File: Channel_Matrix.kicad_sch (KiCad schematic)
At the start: 0 parts

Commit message: progress on switch sheet
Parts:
- added R1601, R1602, R1603, R1604, R1901, R1902, R1903, R1904, R2001, R2101, R2102: 0R, symbol Device:R_Small
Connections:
- net Channel_1: now also R1603.2
- net Channel_2: now also R1604.2
- net Channel_3v3_1: now also R1601.2
- net Channel_3v3_2: now also R1602.2
- net Channel_5V_1: now also R1902.2
- net Channel_5V_2: now also R1901.2
- new net LDO_3V3_3/VOUT: R1904.1
- new net LDO_3V3_4/VOUT: R2102.1
- new net LDO_5V_3/VOUT: R1903.1
- new net LDO_5V_4/VOUT: R2101.1
- new net Switch_CH_3V3_1/VOUT: R1601.1
- new net Switch_CH_3V3_2/VOUT: R1602.1
- new net Switch_CH_3V3_3/VIN: R1903.2, R1904.2
- new net Switch_CH_3V3_3/VOUT: R1603.1, R2001.2
- new net Switch_CH_3V3_5/VIN: R2101.2, R2102.2
- new net Switch_CH_3V3_5/VOUT: R1604.1, R2001.1
- new net Switch_CH_5V_1/VOUT: R1902.1
- new net Switch_CH_5V_2/VOUT: R1901.1
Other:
- removed sheet Switch_CH_3V3_4
- removed sheet Switch_CH_3V3_6
- added sheet LDO_3V3_1 (LDO_3V3.kicad_sch)
- added sheet LDO_3V3_2 (LDO_3V3.kicad_sch)
- added sheet LDO_3V3_3 (LDO_3V3.kicad_sch)
- added sheet LDO_3V3_4 (LDO_3V3.kicad_sch)
- added sheet LDO_5V_1 (LDO_5V.kicad_sch)
- added sheet LDO_5V_2 (LDO_5V.kicad_sch)
- added sheet LDO_5V_3 (LDO_5V.kicad_sch)
- added sheet LDO_5V_4 (LDO_5V.kicad_sch)

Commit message: specified design
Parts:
- removed R1601, R1602, R1903, R1904, R2001, R2101, R2102: 0R, symbol Device:R_Small
- added C2301, C2304: 1u, Capacitor_SMD:C_0603_1608Metric_Pad1.08x0.95mm_HandSolder, symbol Device:C_Small
- added C2302, C2303: 100n, Capacitor_SMD:C_0603_1608Metric_Pad1.08x0.95mm_HandSolder, symbol Device:C_Small
- added C2305: 10u, Capacitor_SMD:C_0603_1608Metric_Pad1.08x0.95mm_HandSolder, symbol Device:C_Small
- added R2302, R2303, R2304, R2306, R2309, R2310: 0R, Resistor_SMD:R_0603_1608Metric_Pad0.98x0.95mm_HandSolder, symbol Device:R_Small
- added U2301: LP38690SDX-3.3/NOPB, Package_SON:WSON-6-1EP_3x3mm_P0.95mm, symbol Regulator_Linear:LP38691SD-3.3
- R2301: renamed from R1604; footprint (none) -> Resistor_SMD:R_0603_1608Metric_Pad0.98x0.95mm_HandSolder
- R2305: renamed from R1603; footprint (none) -> Resistor_SMD:R_0603_1608Metric_Pad0.98x0.95mm_HandSolder
- R2307: renamed from R1902; footprint (none) -> Resistor_SMD:R_0603_1608Metric_Pad0.98x0.95mm_HandSolder
- R2308: renamed from R1901; footprint (none) -> Resistor_SMD:R_0603_1608Metric_Pad0.98x0.95mm_HandSolder
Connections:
- net +5V: now also C2301.1, C2302.1, U2301.1 (IN), U2301.6 (IN)
- net Switch_CH_3V3_3/VOUT renamed Switch_CH_O_1/VOUT
- net Switch_CH_3V3_5/VOUT renamed Switch_CH_O_2/VOUT
- net Switch_CH_5V_1/VOUT renamed Switch_H1/VOUT
- net Switch_CH_5V_2/VOUT renamed Switch_H2/VOUT
- new net +3V3: C2303.1, C2304.1, C2305.1, U2301.4 (OUT), U2301.5 (SNS)
- new net Channel_12V_1: R2309.2
- new net Channel_12V_2: R2310.2
- new net Channel_3: R2306.2
- new net Channel_4: R2302.2
- new net Channel_5: R2303.2
- new net Channel_6: R2304.2
- new net GND: C2301.2, C2302.2, C2303.2, C2304.2, C2305.2, U2301.2 (GND), U2301.7 (EP)
- new net Switch_CH_O_3/VOUT: R2306.1
- new net Switch_CH_O_4/VOUT: R2302.1
- new net Switch_CH_O_5/VOUT: R2303.1
- new net Switch_CH_O_6/VOUT: R2304.1
- new net Switch_CH_O_7/VOUT: R2309.1
- new net Switch_CH_O_8/VOUT: R2310.1
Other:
- sheet LDO_5V_1 renamed 5V_DCDC_7
- sheet LDO_5V_2 renamed 5V_DCDC_8
- sheet LDO_5V_3 renamed 5V_DCDC_1
- sheet LDO_5V_4 renamed 5V_DCDC_2
- removed sheet LDO_3V3_1
- removed sheet LDO_3V3_2
- removed sheet LDO_3V3_3
- removed sheet LDO_3V3_4
- removed sheet Switch_CH_3V3_1
- removed sheet Switch_CH_3V3_2
- removed sheet Switch_CH_3V3_3
- removed sheet Switch_CH_3V3_5
- removed sheet Switch_CH_5V_1
- removed sheet Switch_CH_5V_2
- added sheet 12V_DCDC_1 (12V_DCDC.kicad_sch)
- added sheet 12V_DCDC_2 (12V_DCDC.kicad_sch)
- added sheet 5V_DCDC_3 (LDO_5V.kicad_sch)
- added sheet 5V_DCDC_4 (LDO_5V.kicad_sch)
- added sheet 5V_DCDC_5 (LDO_5V.kicad_sch)
- added sheet 5V_DCDC_6 (LDO_5V.kicad_sch)
- added sheet 5V_DCDC_MCU (LDO_3V3.kicad_sch)
- added sheet Switch_CH_O_1 (Switch_C.kicad_sch)
- added sheet Switch_CH_O_2 (Switch_C.kicad_sch)
- added sheet Switch_CH_O_3 (Switch_C.kicad_sch)
- added sheet Switch_CH_O_4 (Switch_C.kicad_sch)
- added sheet Switch_CH_O_5 (Switch_C.kicad_sch)
- added sheet Switch_CH_O_6 (Switch_C.kicad_sch)
- added sheet Switch_CH_O_7 (Switch_C.kicad_sch)
- added sheet Switch_CH_O_8 (Switch_C.kicad_sch)
- added sheet Switch_H1 (Switch_H.kicad_sch)
- added sheet Switch_H2 (Switch_H.kicad_sch)
- sheet 5V_DCDC_1 ports: added EN; removed none
- sheet 5V_DCDC_2 ports: added EN; removed none
- sheet 5V_DCDC_7 ports: added EN; removed none
- sheet 5V_DCDC_8 ports: added EN; removed none
- note added: "12V channels"
- note added: "3V3/5V channels"
- moved on the sheet: R2301, R2305, R2307, R2308

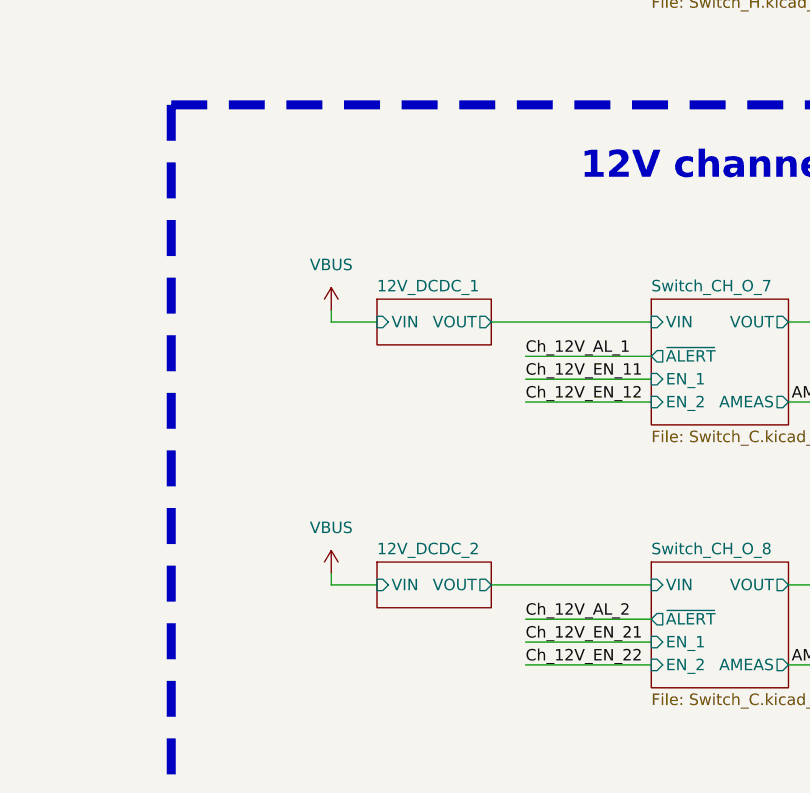
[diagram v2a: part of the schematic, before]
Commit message: added second AMUX and housekeeping
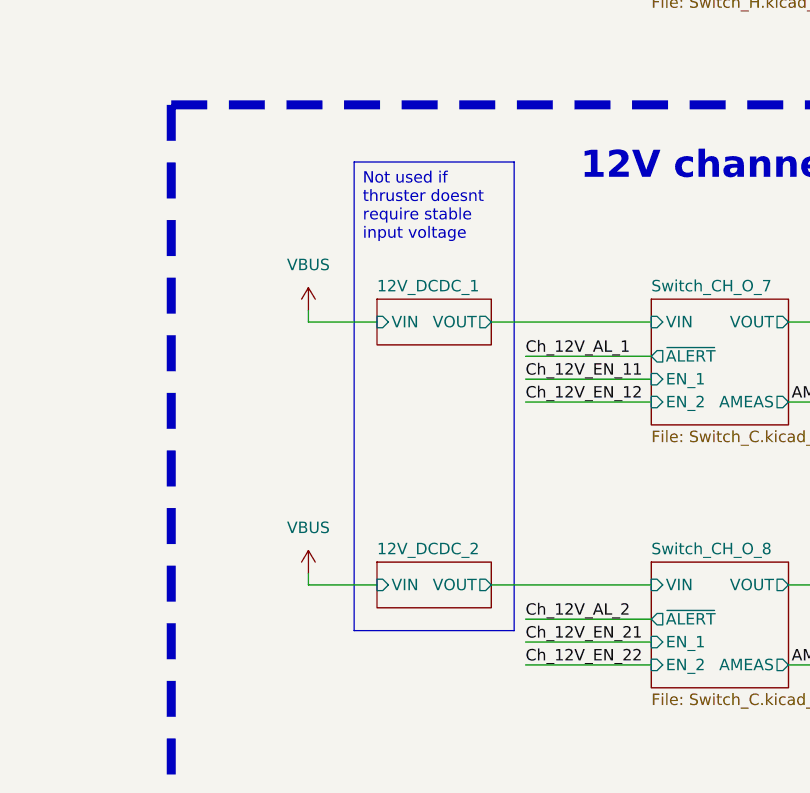
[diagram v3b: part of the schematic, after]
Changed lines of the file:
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@@
 		)
 	)
+	(text_box "Not used if thruster doesnt require stable input voltage"
+		(exclude_from_sim no)
+		(at 196.85 93.98 0)
+		(size 17.78 52.07)
+		(margins 0.9525 0.9525 0.9525 0.9525)
+		(stroke
+			(width 0)
+			(type solid)
+		)
+		(fill
+			(type none)
+		)
+		(effects
+			(font
+				(size 1.27 1.27)
+			)
+			(justify left top)
+		)
+	)
 	(text_box "ke kazde vetvi switch vlastni ldo/dc/dc"
 		(exclude_from_sim no)
@@
 	(wire
 		(pts
-			(xy 194.31 140.97) (xy 199.39 140.97)
+			(xy 191.77 140.97) (xy 199.39 140.97)
 		)
 		(stroke
@@
 	(wire
 		(pts
-			(xy 194.31 110.49) (xy 194.31 111.76)
+			(xy 191.77 110.49) (xy 191.77 111.76)
 		)
 		(stroke
@@
 	(wire
 		(pts
-			(xy 194.31 111.76) (xy 199.39 111.76)
+			(xy 191.77 111.76) (xy 199.39 111.76)
 		)
 		(stroke
@@
 	(wire
 		(pts
-			(xy 194.31 139.7) (xy 194.31 140.97)
+			(xy 191.77 139.7) (xy 191.77 140.97)
 		)
 		(stroke
@@
 	(symbol
 		(lib_id "power:VBUS")
-		(at 194.31 139.7 0)
+		(at 191.77 139.7 0)
 		(unit 1)
 		(exclude_from_sim no)
@@
 		(fields_autoplaced yes)
 		(property "Reference" "#PWR02320"
-			(at 194.31 143.51 0)
+			(at 191.77 143.51 0)
 			(effects
 				(font
@@
 		)
 		(property "Value" "VBUS"
-			(at 194.31 134.62 0)
+			(at 191.77 134.62 0)
 			(effects
 				(font
@@
 		)
 		(property "Footprint" ""
-			(at 194.31 139.7 0)
+			(at 191.77 139.7 0)
 			(effects
 				(font
@@
 		)
 		(property "Datasheet" ""
-			(at 194.31 139.7 0)
+			(at 191.77 139.7 0)
 			(effects
 				(font
@@
 		)
 		(property "Description" "Power symbol creates a global label with name \"VBUS\""
-			(at 194.31 139.7 0)
+			(at 191.77 139.7 0)
 			(effects
 				(font
@@
 	(symbol
 		(lib_id "power:VBUS")
-		(at 194.31 110.49 0)
+		(at 191.77 110.49 0)
 		(unit 1)
 		(exclude_from_sim no)
@@
 		(fields_autoplaced yes)
 		(property "Reference" "#PWR02319"
-			(at 194.31 114.3 0)
+			(at 191.77 114.3 0)
 			(effects
 				(font
@@
 		)
 		(property "Value" "VBUS"
-			(at 194.31 105.41 0)
+			(at 191.77 105.41 0)
 			(effects
 				(font
@@
 		)
 		(property "Footprint" ""
-			(at 194.31 110.49 0)
+			(at 191.77 110.49 0)
 			(effects
 				(font
@@
 		)
 		(property "Datasheet" ""
-			(at 194.31 110.49 0)
+			(at 191.77 110.49 0)
 			(effects
 				(font
@@
 		)
 		(property "Description" "Power symbol creates a global label with name \"VBUS\""
-			(at 194.31 110.49 0)
+			(at 191.77 110.49 0)
 			(effects
 				(font

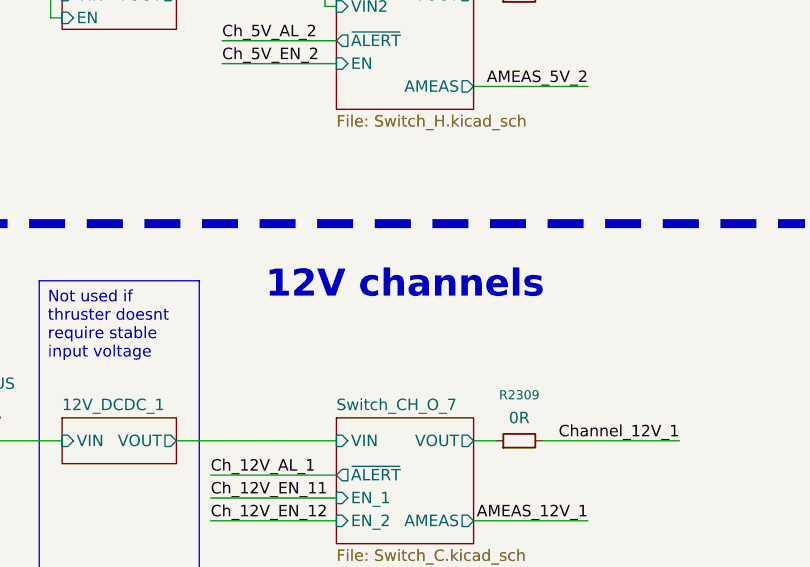
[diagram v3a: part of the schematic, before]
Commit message: connected CAN driver, added 3 solar inputs
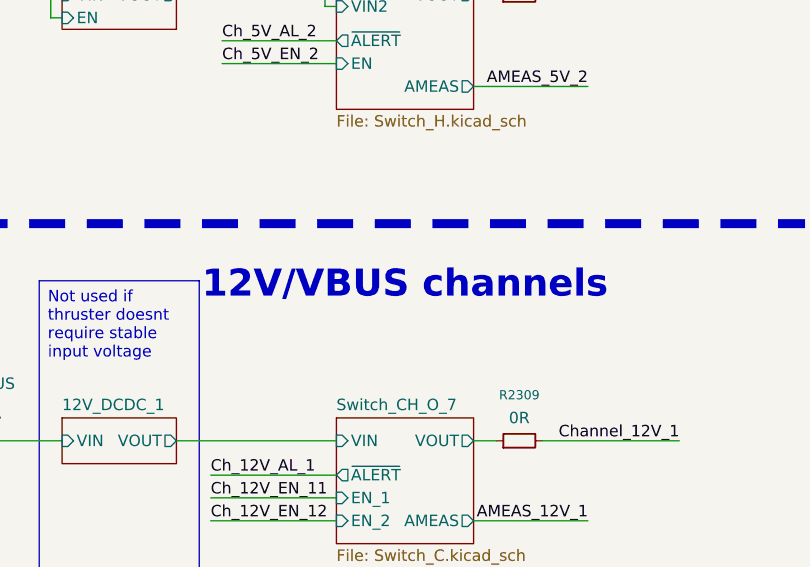
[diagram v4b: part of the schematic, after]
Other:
- note added: "12V/VBUS channels"
- note removed: "12V channels"
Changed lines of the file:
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@@
 	(generator_version "9.0")
 	(paper "A4")
-	(text "12V channels"
+	(text "12V/VBUS channels"
 		(exclude_from_sim no)
 		(at 237.49 94.488 0)

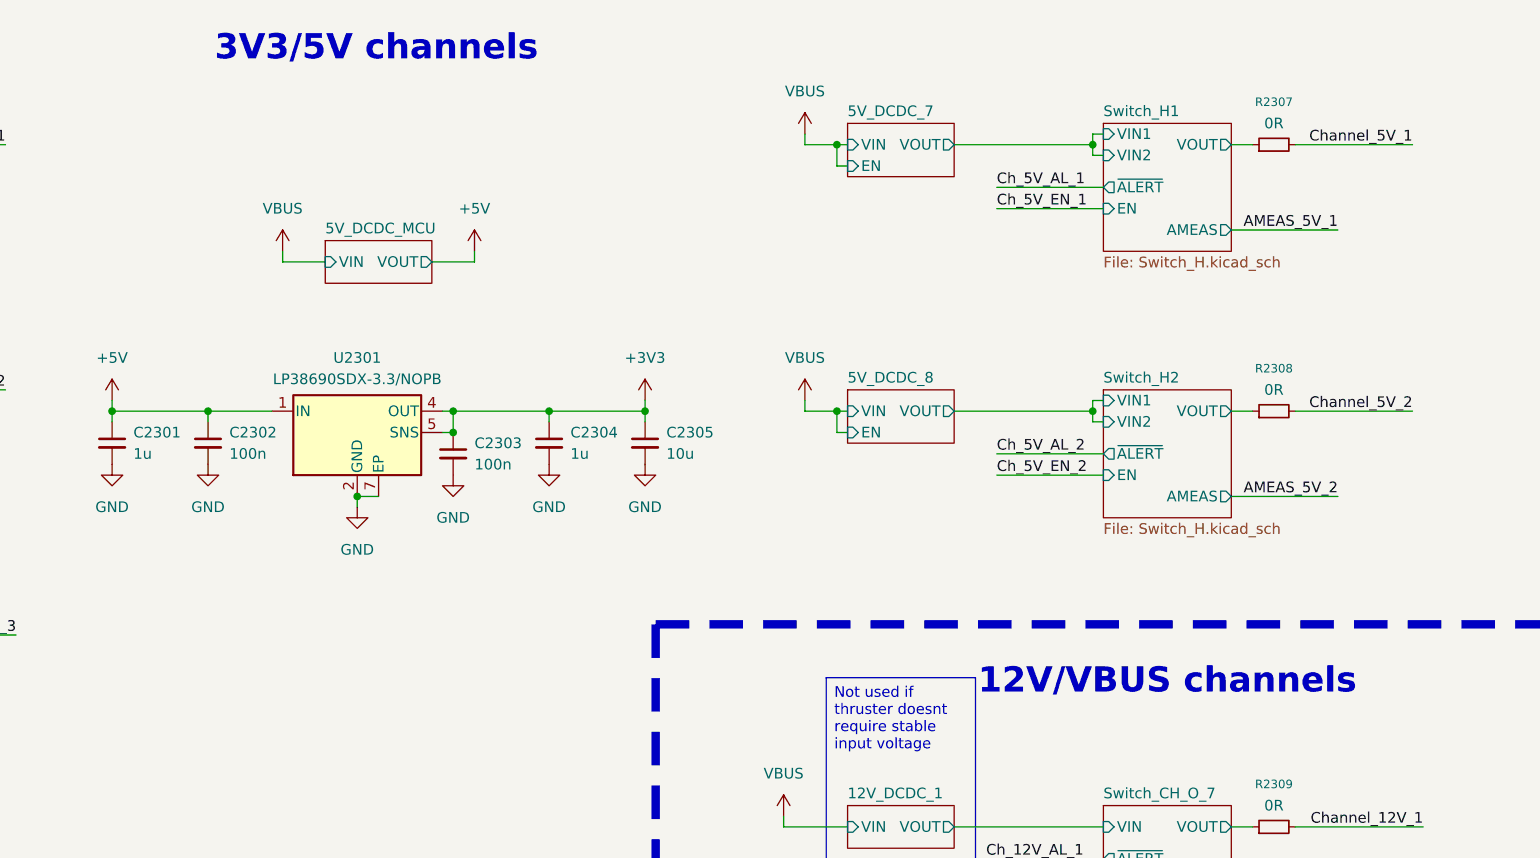
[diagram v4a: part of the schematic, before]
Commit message: added possible solutions for mppt
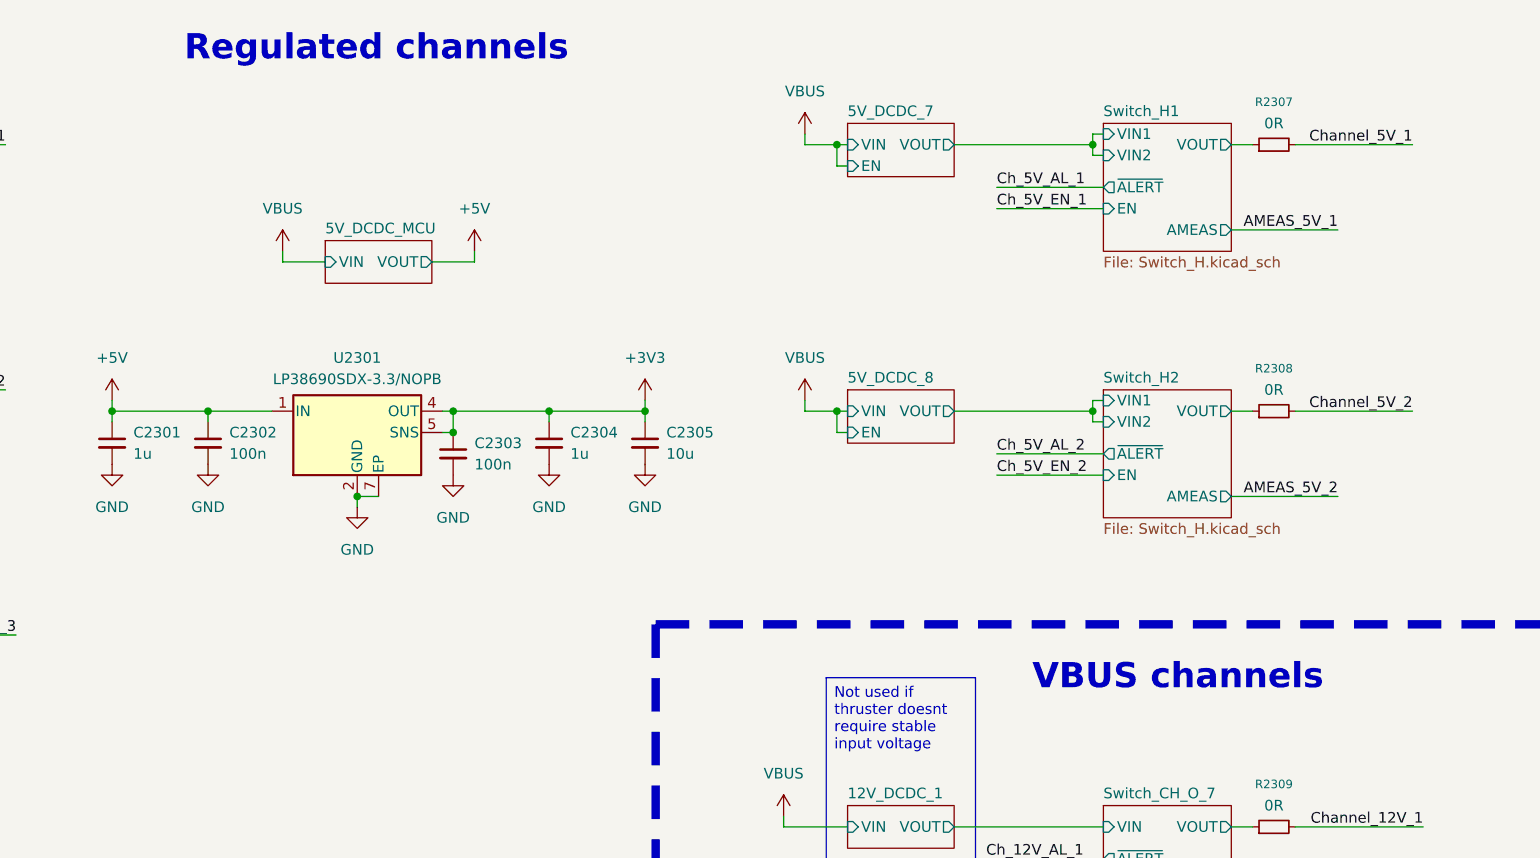
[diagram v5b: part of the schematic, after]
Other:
- note added: "Regulated channels"
- note added: "VBUS channels"
- note removed: "12V/VBUS channels"
- note removed: "3V3/5V channels"
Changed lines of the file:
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@@
 	(generator_version "9.0")
 	(paper "A4")
-	(text "12V/VBUS channels"
+	(text "VBUS channels"
 		(exclude_from_sim no)
-		(at 237.49 94.488 0)
+		(at 238.76 93.98 0)
 		(effects
 			(font
@@
 		)
 	)
-	(text "3V3/5V channels"
+	(text "Regulated channels"
 		(exclude_from_sim no)
 		(at 143.256 19.05 0)

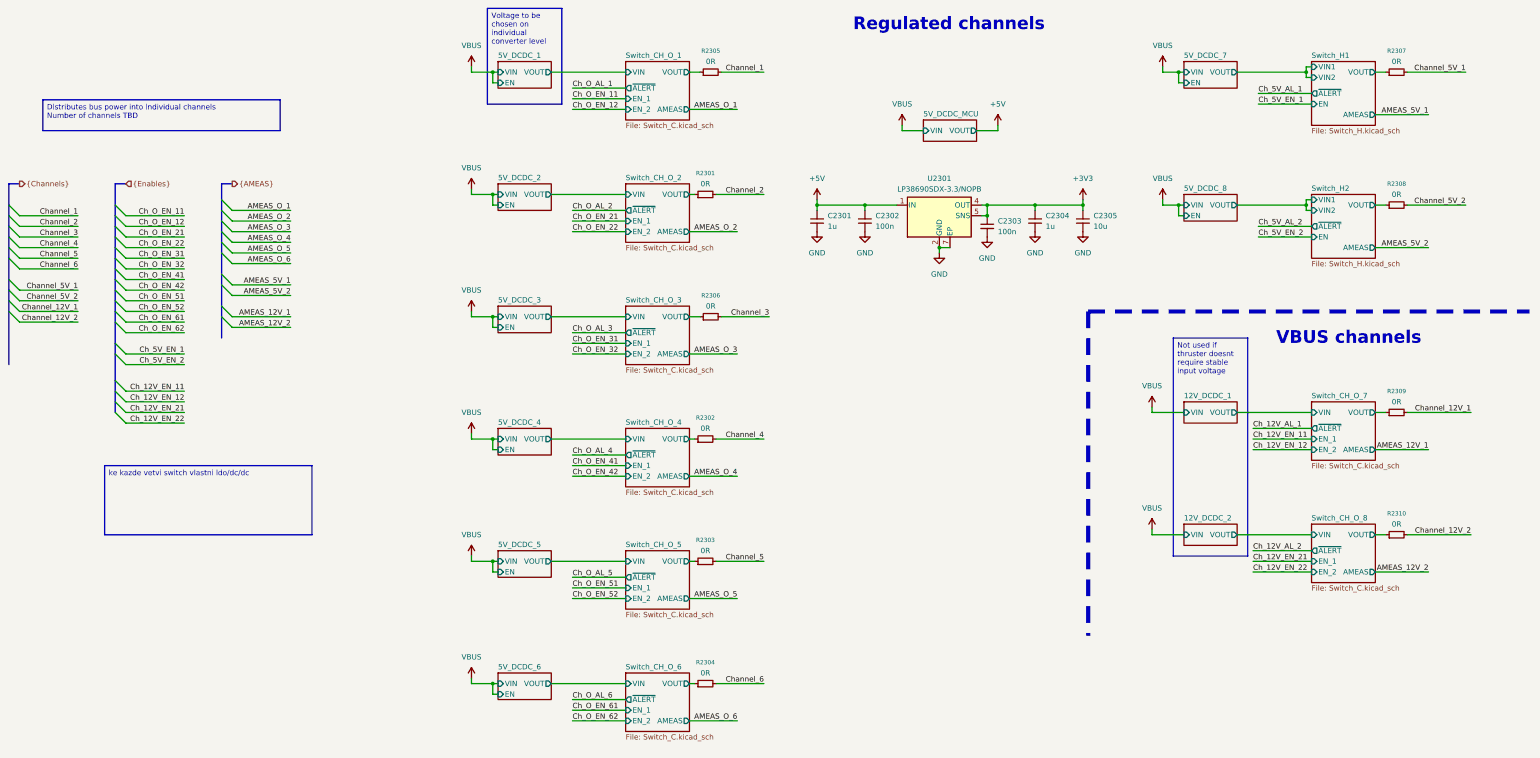
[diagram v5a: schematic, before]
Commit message: changed IO epanders to 2nd MSP430
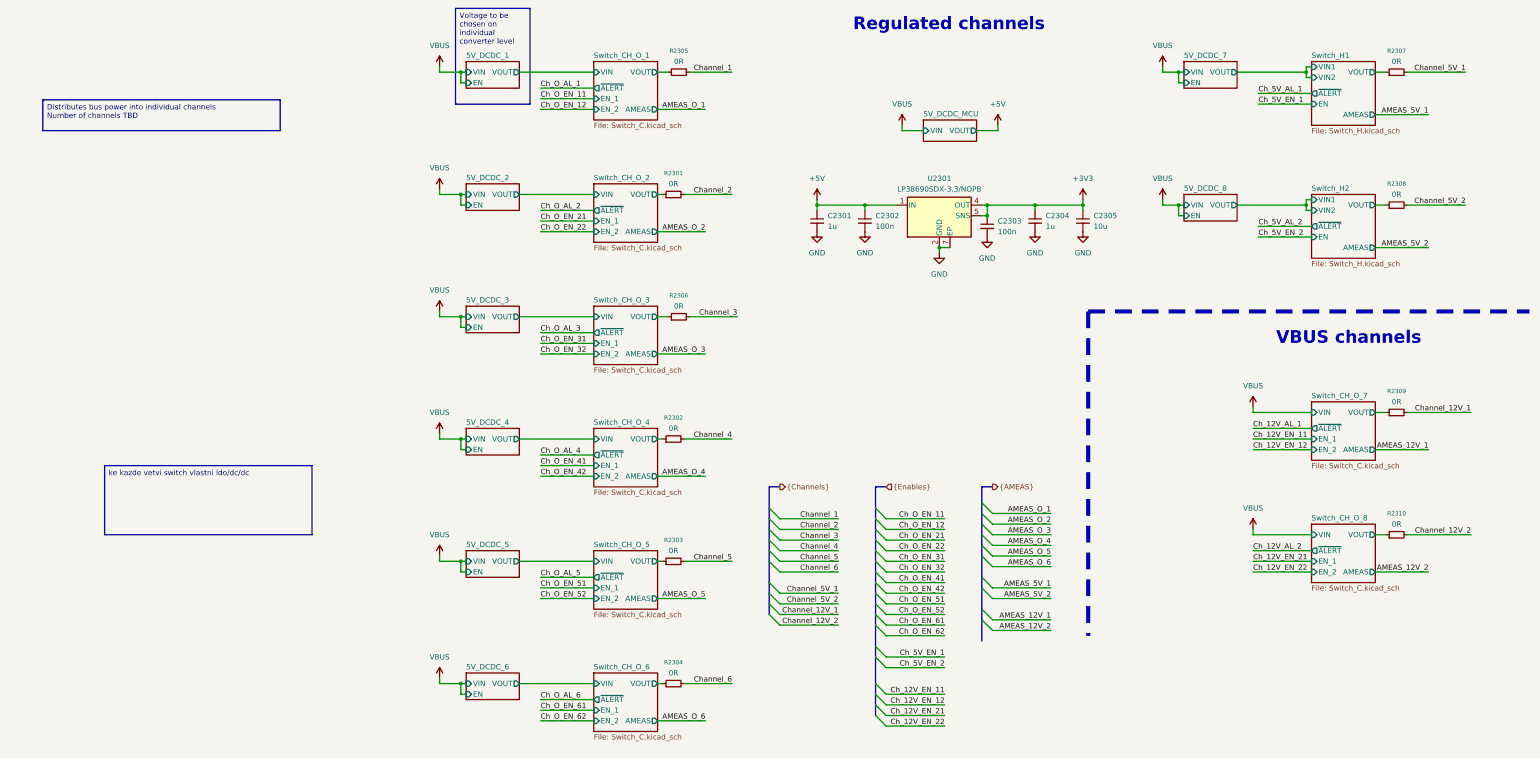
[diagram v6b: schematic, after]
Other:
- removed sheet 12V_DCDC_1
- removed sheet 12V_DCDC_2
- moved on the sheet: R2301, R2302, R2303, R2304, R2305, R2306
